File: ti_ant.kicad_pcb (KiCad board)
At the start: 2 copper layers, 13 x 18 mm, 3 parts

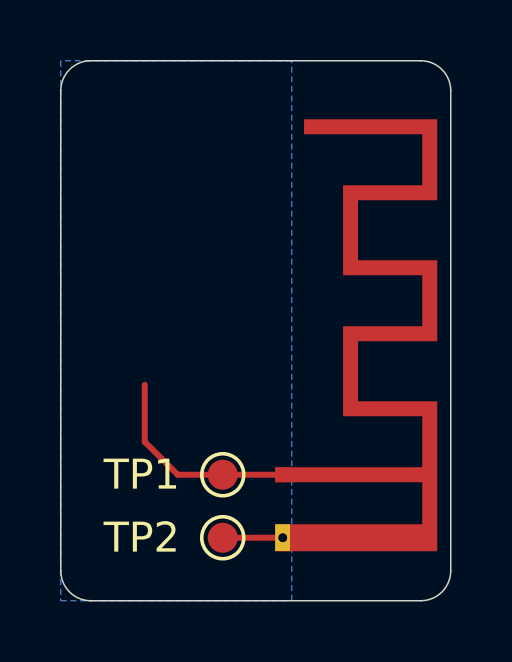
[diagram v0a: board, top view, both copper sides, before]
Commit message: Simplify test model
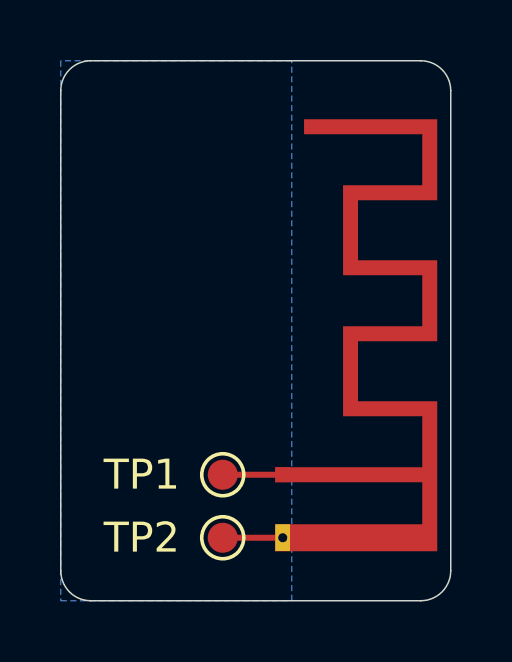
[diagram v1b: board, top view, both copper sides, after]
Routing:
- net Net-(AE1-Pad1): track 6.96 -> 2.00 mm
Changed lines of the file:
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@@
   (gr_line (start 136.875 86.15) (end 147.875 86.15)
     (stroke (width 0.05) (type default)) (layer "Edge.Cuts"))
-  (segment (start 139.775 99.95) (end 138.675 98.85) (width 0.2) (layer "F.Cu") (net 1))
-  (segment (start 141.275 99.95) (end 139.775 99.95) (width 0.2) (layer "F.Cu") (net 1))
   (segment (start 143.275 99.95) (end 141.275 99.95) (width 0.2) (layer "F.Cu") (net 1))
-  (segment (start 138.675 98.85) (end 138.675 96.95) (width 0.2) (layer "F.Cu") (net 1))
   (segment (start 143.275 102.05) (end 141.275 102.05) (width 0.2) (layer "F.Cu") (net 2))
   (zone (net 2) (net_name "GND") (layer "B.Cu") (hatch edge 0.5)
